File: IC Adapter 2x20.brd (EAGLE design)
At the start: 23 x 53 mm, 4 parts, among them IC3 LTC6804IG-1#PBF

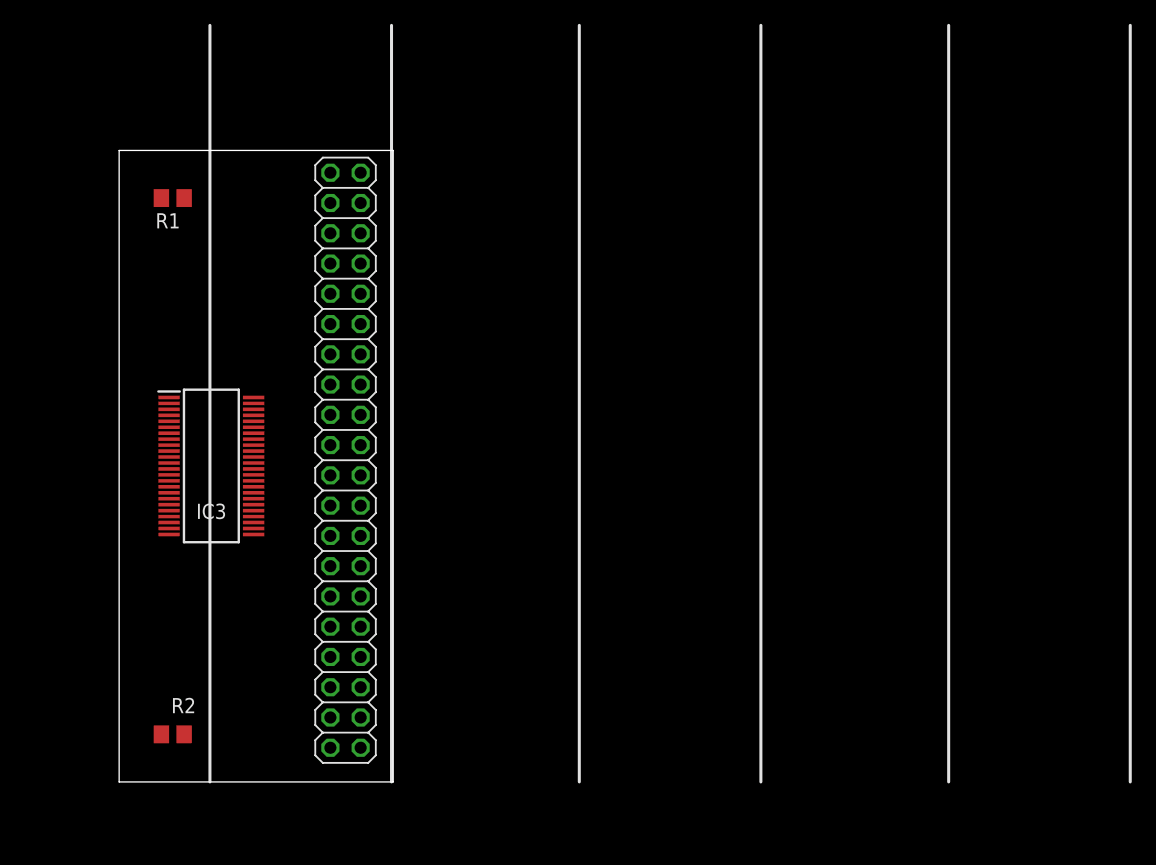
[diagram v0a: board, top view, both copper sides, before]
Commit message: IC adapter layouted
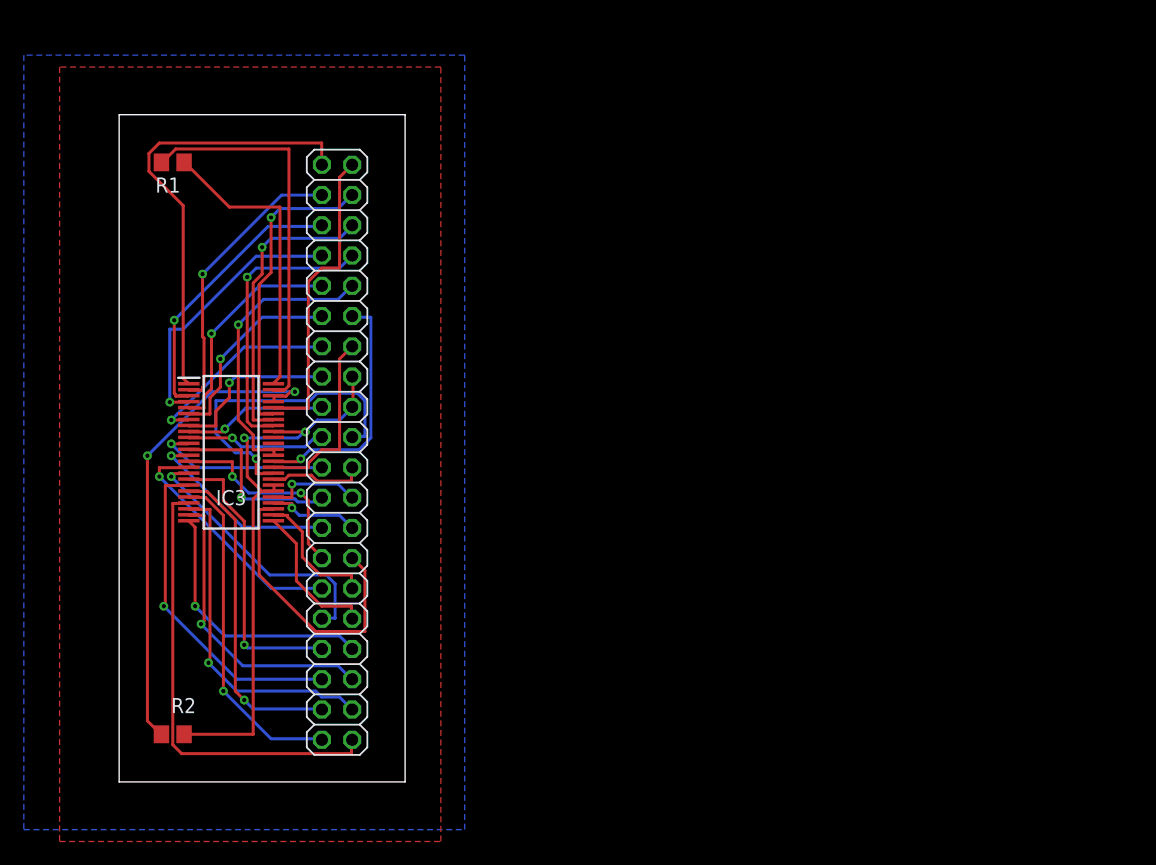
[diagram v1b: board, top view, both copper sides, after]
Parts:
- moved R1 3.00 mm to (4.50, 52.0)
- moved IC3 2.02 mm to (9.40, 27.7)
- moved JP1 0.98 mm to (18.3, 27.7)
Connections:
- net GPIO1: now also JP1.28; no longer JP1.20
- net GPIO2: now also JP1.26; no longer JP1.22
- net GPIO4: now also JP1.22; no longer JP1.26
- net GPIO5: now also JP1.20; no longer JP1.28
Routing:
- net GND: track 0.00 -> 48.6 mm, vias 0 -> 2
- net ICMP: track 0.00 -> 40.9 mm, vias 0 -> 2
- net S3: track 0.00 -> 38.1 mm
- net V+: track 0.00 -> 37.4 mm
- net N$2: track 0.00 -> 32.5 mm
- net C2: track 0.00 -> 28.4 mm, vias 0 -> 1
- net C3: track 0.00 -> 28.3 mm, vias 0 -> 1
- net C4: track 0.00 -> 28.0 mm, vias 0 -> 1
- net S4: track 0.00 -> 27.2 mm, vias 0 -> 1
- net GPIO5: track 0.00 -> 26.8 mm, vias 0 -> 1
- net SDO: track 0.00 -> 25.8 mm
- net SDI: track 0.00 -> 25.7 mm, vias 0 -> 1
- net S2: track 0.00 -> 25.1 mm, vias 0 -> 1
- net SCK: track 0.00 -> 24.9 mm, vias 0 -> 1
- net N$1: track 0.00 -> 24.7 mm
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- added copper zone on layer 1, net GND
- added copper zone on layer 16, net GND
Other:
- board size 23 x 53 mm -> 24 x 56 mm

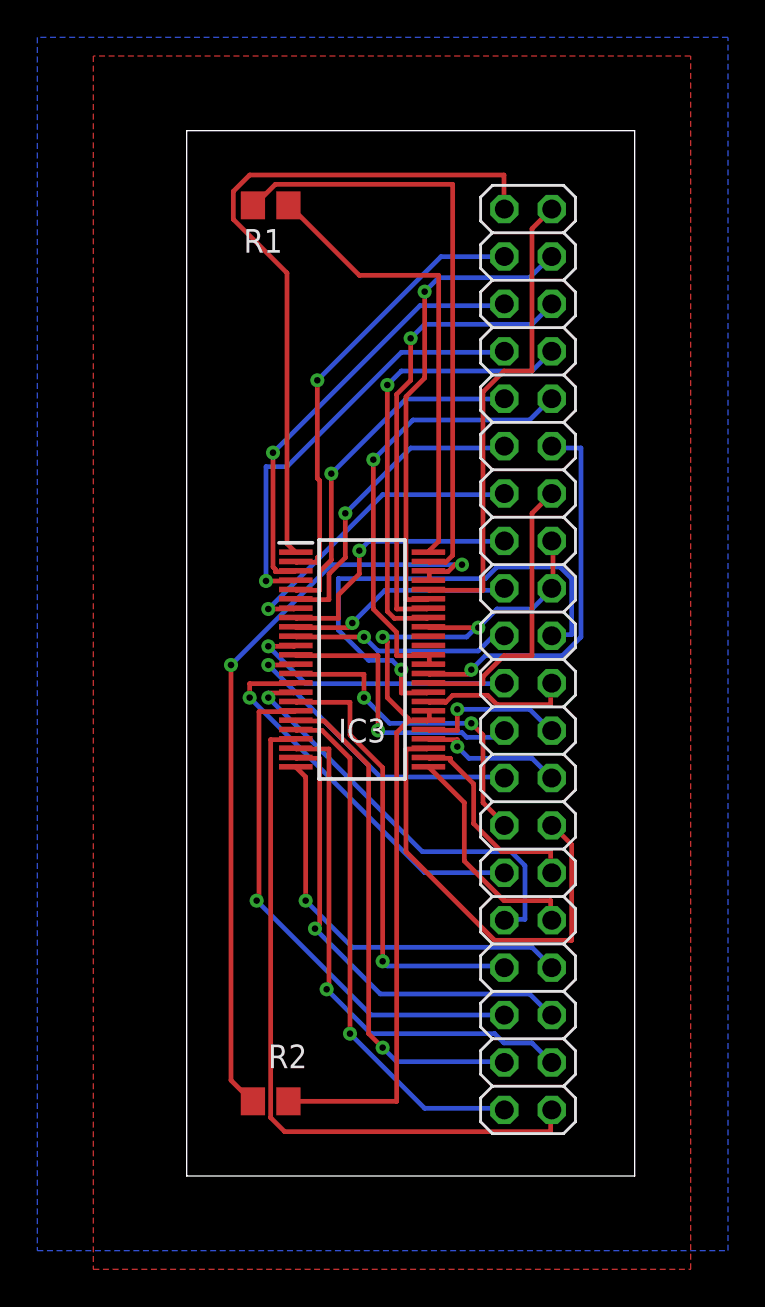
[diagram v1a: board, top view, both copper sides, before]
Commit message: new routing of small IC Adapter
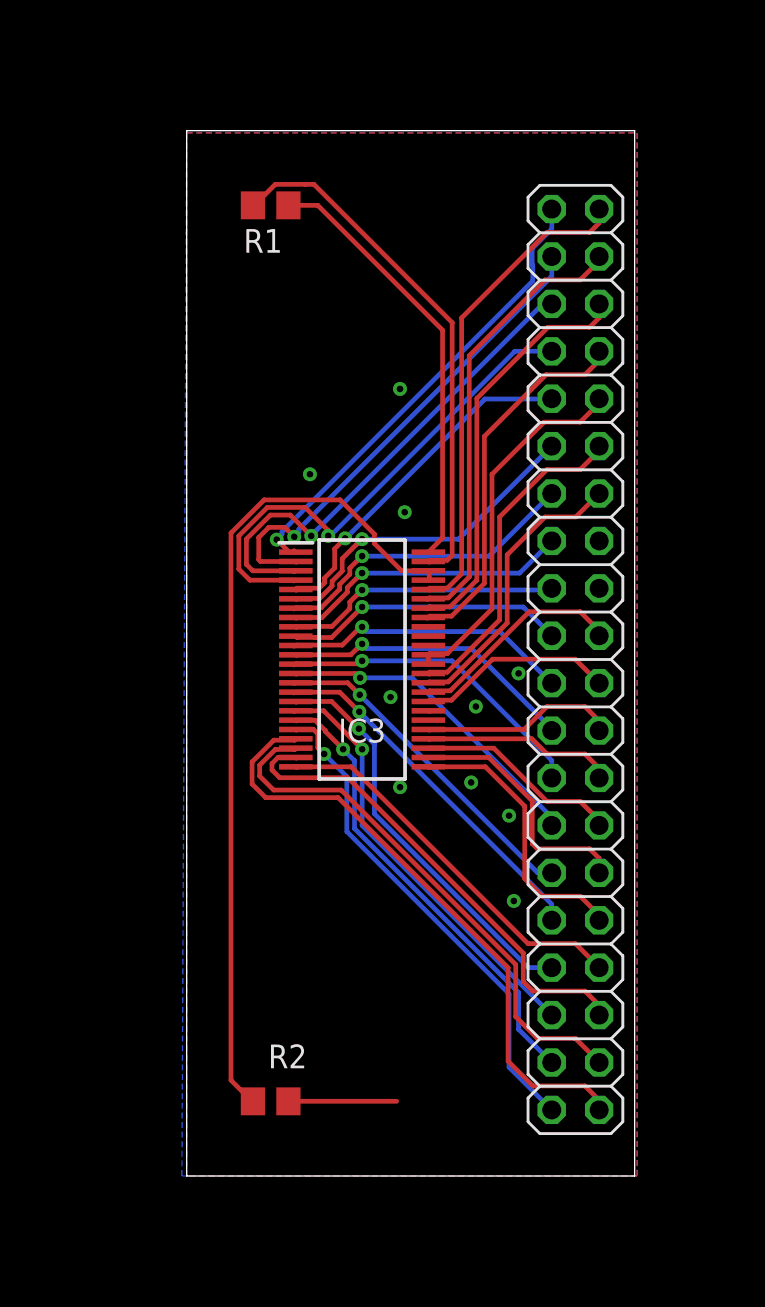
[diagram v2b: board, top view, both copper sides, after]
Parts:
- moved JP1 2.54 mm to (20.8, 27.7)
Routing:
- net GND: track 48.6 -> 5.99 mm, vias 2 -> 10
- net GPIO5: track 26.8 -> 11.6 mm, vias 1 -> 0
- net GPIO1: track 24.2 -> 11.0 mm
- net V+: track 37.4 -> 25.3 mm, vias 0 -> 1
- net C4: track 28.0 -> 23.0 mm
- net S3: track 38.1 -> 33.2 mm
- net C11: track 23.1 -> 27.5 mm
- net N$2: track 32.5 -> 28.2 mm
- net VREG: track 24.2 -> 19.9 mm, vias 1 -> 0
- net CSB: track 24.0 -> 20.0 mm, vias 1 -> 0
- net C5: track 23.2 -> 19.4 mm
- net ICMP: track 40.9 -> 44.7 mm, vias 2 -> 0
- net S12: track 23.3 -> 26.8 mm
- net VREF1: track 20.9 -> 17.6 mm, vias 1 -> 0
- net C8: track 11.9 -> 15.1 mm
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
